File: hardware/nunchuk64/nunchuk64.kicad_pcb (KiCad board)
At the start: 2 copper layers, 50 x 41.6 mm, 40 parts, among them J1 DB9_Female, J2 DB9_Female, J3 Conn_02x03_Odd_Even, P1 CONN_WII, P2 CONN_WII, Q1 BSS138, Q2 BSS138, Q3 BSS138, Q4 BSS138, SW1 SW_Push, U1 AMS1117-3V3, U2 ATMEGA328P-AU

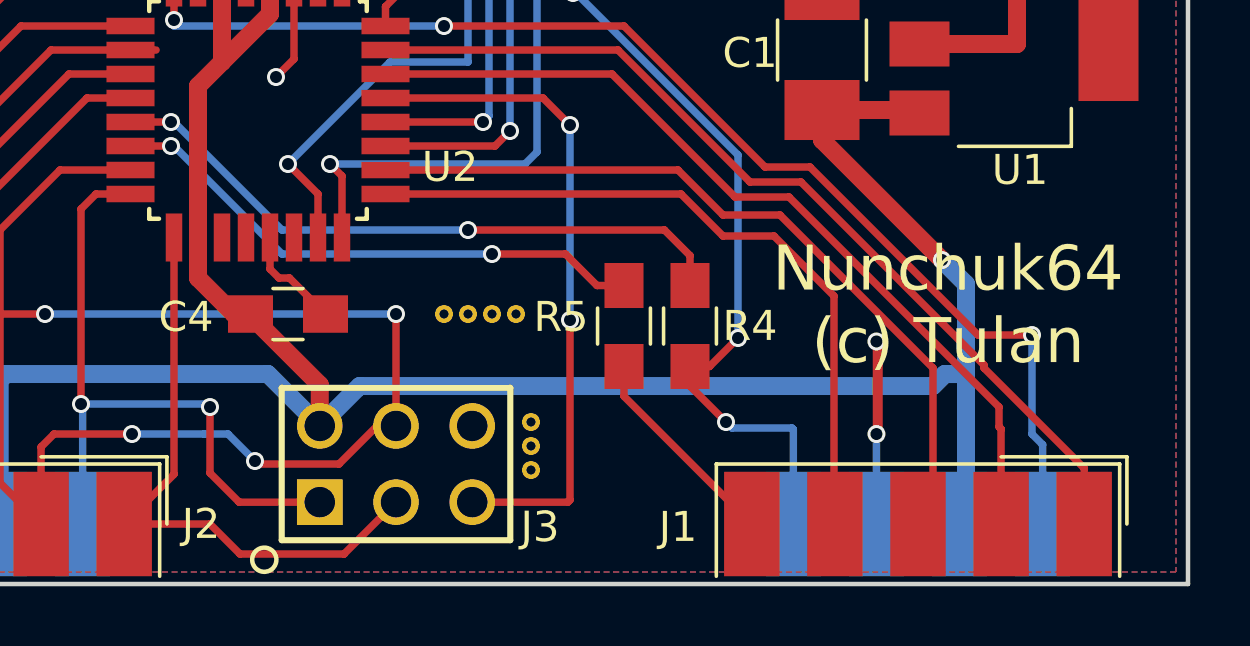
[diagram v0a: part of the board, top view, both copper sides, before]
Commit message: added cosmetic change in layout
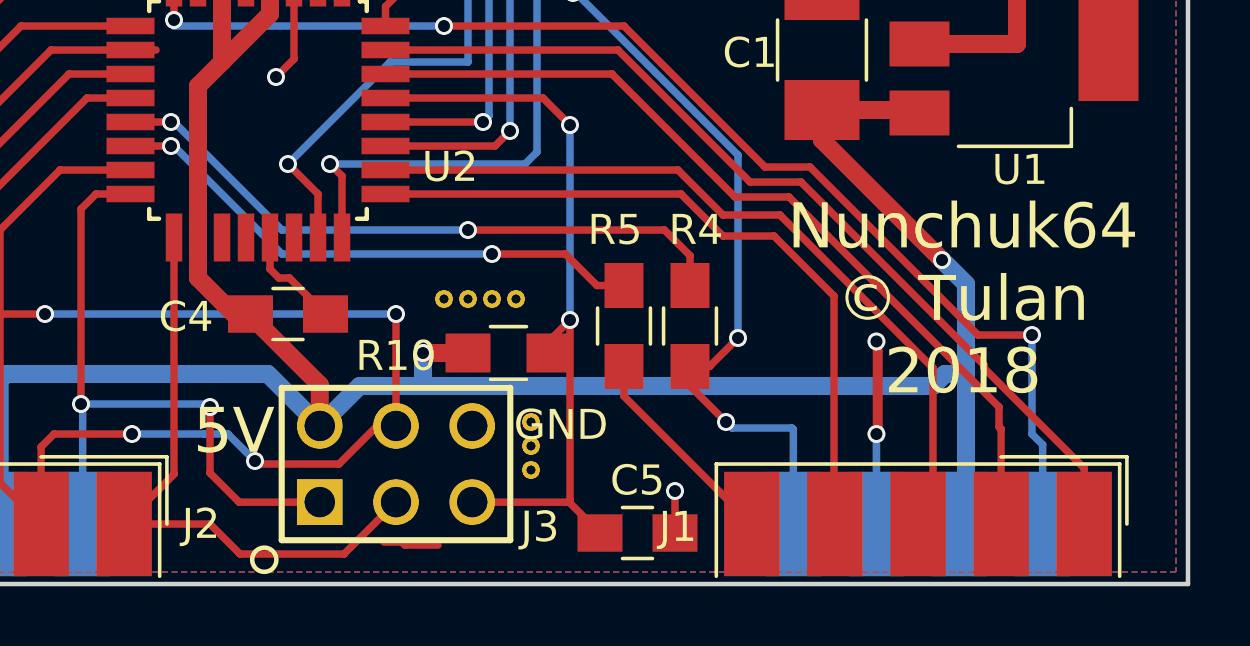
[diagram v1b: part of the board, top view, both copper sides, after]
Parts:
- added C5: 100nF, Capacitors_SMD:C_0805_HandSoldering, F.Cu at (108.0, 111.9)
- added R10: 10k, Resistors_SMD:R_0805_HandSoldering, F.Cu at (103.8, 105.9)
- moved ? 0.50 mm to (103.2, 104.1)
- moved ? 0.50 mm to (104.0, 104.1)
- moved ? 0.50 mm to (101.6, 104.1)
- moved ? 0.50 mm to (102.4, 104.1)
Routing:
- net /RESET: track 22.3 -> 25.2 mm
- net +5V: track 82.4 -> 85.0 mm, vias 1 -> 2
- net (no net): track 0.00 -> 1.84 mm
- net GND: track 23.6 -> 25.0 mm, vias 4 -> 5
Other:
- board text added: "5V"
- board text added: "GND"
- board text added: "Nunchuk64 © Tulan 2018"
- board text removed: "Nunchuk64 (c) Tulan"
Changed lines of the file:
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@@
 (kicad_pcb (version 4) (host pcbnew 4.0.7-e2-6376~58~ubuntu17.04.1)
   (general
-    (links 89)
-    (no_connects 0)
-    (area 69.224999 69.666999 133.575001 129.535)
+    (links 93)
+    (no_connects 1)
+    (area 76.324999 71.924999 126.475001 113.675001)
     (thickness 1.6)
-    (drawings 10)
-    (tracks 350)
+    (drawings 12)
+    (tracks 363)
     (zones 0)
-    (modules 40)
+    (modules 42)
     (nets 42)
   )
@@
     (tags "resistor 0805")
     (attr smd)
-    (fp_text reference R4 (at 0 -2 360) (layer F.SilkS)
+    (fp_text reference R4 (at -3.2 -0.2 360) (layer F.SilkS)
       (effects (font (size 1 1) (thickness 0.15)))
     )
@@
     (tags "resistor 0805")
     (attr smd)
-    (fp_text reference R5 (at -0.3 2.1 360) (layer F.SilkS)
+    (fp_text reference R5 (at -3.2 0.3 360) (layer F.SilkS)
       (effects (font (size 1 1) (thickness 0.15)))
     )
@@
   )
   (module nunchuk_commodore:VIA-0.6mm (layer F.Cu)
-    (at 101.6 104.6)
+    (at 101.6 104.1)
     (fp_text reference "" (at 0 1.524) (layer F.SilkS) hide
       (effects (font (size 1 1) (thickness 0.15)))
@@
   )
   (module nunchuk_commodore:VIA-0.6mm (layer F.Cu)
-    (at 102.4 104.6)
+    (at 102.4 104.1)
     (fp_text reference "" (at 0 1.524) (layer F.SilkS) hide
       (effects (font (size 1 1) (thickness 0.15)))
@@
   )
   (module nunchuk_commodore:VIA-0.6mm (layer F.Cu)
-    (at 103.2 104.6)
+    (at 103.2 104.1)
     (fp_text reference "" (at 0 1.524) (layer F.SilkS) hide
       (effects (font (size 1 1) (thickness 0.15)))
@@
   )
   (module nunchuk_commodore:VIA-0.6mm (layer F.Cu)
-    (at 104 104.6)
+    (at 104 104.1)
     (fp_text reference "" (at 0 1.524) (layer F.SilkS) hide
       (effects (font (size 1 1) (thickness 0.15)))
@@
       (net 8 GND) (zone_connect 2))
   )
-  (gr_text "Nunchuk64\n(c) Tulan" (at 118.4 104.3) (layer F.SilkS)
+  (module Capacitors_SMD:C_0805_HandSoldering (layer F.Cu)
+    (at 108.05 111.9)
+    (descr "Capacitor SMD 0805, hand soldering")
+    (tags "capacitor 0805")
+    (attr smd)
+    (fp_text reference C5 (at 0 -1.75) (layer F.SilkS)
+      (effects (font (size 1 1) (thickness 0.15)))
+    )
+    (fp_text value 100nF (at 0 1.75) (layer F.Fab)
+      (effects (font (size 1 1) (thickness 0.15)))
+    )
+    (fp_text user %R (at 0 -1.75) (layer F.Fab)
+      (effects (font (size 1 1) (thickness 0.15)))
+    )
+    (fp_line (start -1 0.62) (end -1 -0.62) (layer F.Fab) (width 0.1))
+    (fp_line (start 1 0.62) (end -1 0.62) (layer F.Fab) (width 0.1))
+    (fp_line (start 1 -0.62) (end 1 0.62) (layer F.Fab) (width 0.1))
+    (fp_line (start -1 -0.62) (end 1 -0.62) (layer F.Fab) (width 0.1))
+    (fp_line (start 0.5 -0.85) (end -0.5 -0.85) (layer F.SilkS) (width 0.12))
+    (fp_line (start -0.5 0.85) (end 0.5 0.85) (layer F.SilkS) (width 0.12))
+    (fp_line (start -2.25 -0.88) (end 2.25 -0.88) (layer F.CrtYd) (width 0.05))
+    (fp_line (start -2.25 -0.88) (end -2.25 0.87) (layer F.CrtYd) (width 0.05))
+    (fp_line (start 2.25 0.87) (end 2.25 -0.88) (layer F.CrtYd) (width 0.05))
+    (fp_line (start 2.25 0.87) (end -2.25 0.87) (layer F.CrtYd) (width 0.05))
+    (pad 1 smd rect (at -1.25 0) (size 1.5 1.25) (layers F.Cu F.Paste F.Mask)
+      (net 35 /RESET))
+    (pad 2 smd rect (at 1.25 0) (size 1.5 1.25) (layers F.Cu F.Paste F.Mask)
+      (net 8 GND))
+    (model Capacitors_SMD.3dshapes/C_0805.wrl
+      (at (xyz 0 0 0))
+      (scale (xyz 1 1 1))
+      (rotate (xyz 0 0 0))
+    )
+  )
+  (module Resistors_SMD:R_0805_HandSoldering (layer F.Cu)
+    (at 103.75 105.9)
+    (descr "Resistor SMD 0805, hand soldering")
+    (tags "resistor 0805")
+    (attr smd)
+    (fp_text reference R10 (at -3.75 0.1) (layer F.SilkS)
+      (effects (font (size 1 1) (thickness 0.15)))
+    )
+    (fp_text value 10k (at 0 1.75) (layer F.Fab)
+      (effects (font (size 1 1) (thickness 0.15)))
+    )
+    (fp_text user %R (at 0 0) (layer F.Fab)
+      (effects (font (size 0.5 0.5) (thickness 0.075)))
+    )
+    (fp_line (start -1 0.62) (end -1 -0.62) (layer F.Fab) (width 0.1))
+    (fp_line (start 1 0.62) (end -1 0.62) (layer F.Fab) (width 0.1))
+    (fp_line (start 1 -0.62) (end 1 0.62) (layer F.Fab) (width 0.1))
+    (fp_line (start -1 -0.62) (end 1 -0.62) (layer F.Fab) (width 0.1))
+    (fp_line (start 0.6 0.88) (end -0.6 0.88) (layer F.SilkS) (width 0.12))
+    (fp_line (start -0.6 -0.88) (end 0.6 -0.88) (layer F.SilkS) (width 0.12))
+    (fp_line (start -2.35 -0.9) (end 2.35 -0.9) (layer F.CrtYd) (width 0.05))
+    (fp_line (start -2.35 -0.9) (end -2.35 0.9) (layer F.CrtYd) (width 0.05))
+    (fp_line (start 2.35 0.9) (end 2.35 -0.9) (layer F.CrtYd) (width 0.05))
+    (fp_line (start 2.35 0.9) (end -2.35 0.9) (layer F.CrtYd) (width 0.05))
+    (pad 1 smd rect (at -1.35 0) (size 1.5 1.3) (layers F.Cu F.Paste F.Mask)
+      (net 7 +5V))
+    (pad 2 smd rect (at 1.35 0) (size 1.5 1.3) (layers F.Cu F.Paste F.Mask)
+      (net 35 /RESET))
+    (model ${KISYS3DMOD}/Resistors_SMD.3dshapes/R_0805.wrl
+      (at (xyz 0 0 0))
+      (scale (xyz 1 1 1))
+      (rotate (xyz 0 0 0))
+    )
+  )
+  (gr_text 5V (at 94.6 108.5) (layer F.SilkS)
+    (effects (font (size 1.5 1.5) (thickness 0.3)))
+  )
+  (gr_text GND (at 105.5 108.3) (layer F.SilkS)
+    (effects (font (size 1 1) (thickness 0.25)))
+  )
+  (gr_text "Nunchuk64\n© Tulan\n2018" (at 118.9 104.1) (layer F.SilkS)
     (effects (font (size 1.5 1.5) (thickness 0.3)))
   )
@@
   (gr_line (start 126.4 113.6) (end 126.4 72) (angle 90) (layer Eco1.User) (width 0.2))
   (gr_line (start 76.4 72) (end 76.4 113.6) (angle 90) (layer Eco1.User) (width 0.2))
+  (segment (start 100.3 112.3) (end 101.4 112.3) (width 0.25) (layer F.Cu) (net 0))
+  (segment (start 100.2 112.2) (end 100.3 112.3) (width 0.25) (layer F.Cu) (net 0))
+  (segment (start 99.6 112.2) (end 100.2 112.2) (width 0.25) (layer F.Cu) (net 0))
   (segment (start 122.94 111.6) (end 122.94 109.74) (width 0.25) (layer F.Cu) (net 1))
   (segment (start 122.94 109.74) (end 119.6 106.4) (width 0.25) (layer F.Cu) (net 1))
@@
   (segment (start 92.6 94.8) (end 92.6 93.55) (width 0.25) (layer F.Cu) (net 6))
   (via (at 92.6 94.8) (size 0.6) (drill 0.4) (layers F.Cu B.Cu) (net 6))
+  (segment (start 100.9 105.9) (end 102.4 105.9) (width 0.6) (layer F.Cu) (net 7))
+  (segment (start 100.9 107) (end 98.79 107) (width 0.6) (layer B.Cu) (net 7))
+  (segment (start 117.9 107) (end 100.9 107) (width 0.6) (layer B.Cu) (net 7))
+  (segment (start 100.9 107) (end 100.9 105.9) (width 0.6) (layer B.Cu) (net 7))
+  (via (at 100.9 105.9) (size 0.6) (drill 0.4) (layers F.Cu B.Cu) (net 7))
   (segment (start 118.3 106.6) (end 117.9 107) (width 0.6) (layer B.Cu) (net 7))
-  (segment (start 117.9 107) (end 98.79 107) (width 0.6) (layer B.Cu) (net 7))
   (segment (start 98.79 107) (end 97.46 108.33) (width 0.6) (layer B.Cu) (net 7))
   (segment (start 118.9 106.6) (end 118.3 106.6) (width 0.6) (layer B.Cu) (net 7))
@@
   (segment (start 94.2 96.2) (end 94.2 93.55) (width 0.6) (layer F.Cu) (net 7))
   (segment (start 93.4 102.05) (end 93.4 102.85) (width 0.25) (layer F.Cu) (net 7))
+  (via (at 109.3 110.5) (size 0.6) (drill 0.4) (layers F.Cu B.Cu) (net 8))
+  (segment (start 109.3 111.9) (end 109.3 110.5) (width 0.25) (layer F.Cu) (net 8))
   (via (at 116.015 105.515) (size 0.6) (drill 0.4) (layers F.Cu B.Cu) (net 8))
   (segment (start 116.015 108.6) (end 116.015 105.515) (width 0.25) (layer F.Cu) (net 8))
@@
   (segment (start 79.8 102.7) (end 87.5 95) (width 0.25) (layer F.Cu) (net 31))
   (segment (start 87.5 95) (end 91.15 95) (width 0.25) (layer F.Cu) (net 31))
+  (segment (start 105.1 105.9) (end 105.1 105.5) (width 0.25) (layer F.Cu) (net 35))
+  (segment (start 105.1 105.5) (end 105.8 104.8) (width 0.25) (layer F.Cu) (net 35))
+  (segment (start 105.73 110.87) (end 105.77 110.87) (width 0.25) (layer F.Cu) (net 35))
+  (segment (start 105.77 110.87) (end 106.8 111.9) (width 0.25) (layer F.Cu) (net 35))
   (segment (start 105.8 104.8) (end 105.8 110.8) (width 0.25) (layer F.Cu) (net 35))
   (segment (start 105.8 110.8) (end 105.73 110.87) (width 0.25) (layer F.Cu) (net 35))

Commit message: changed layout a bit
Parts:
- moved R10 0.75 mm to (104.5, 105.9)
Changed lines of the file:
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@@
   (general
     (links 93)
-    (no_connects 1)
+    (no_connects 0)
     (area 76.324999 71.924999 126.475001 113.675001)
     (thickness 1.6)
     (drawings 12)
-    (tracks 363)
+    (tracks 364)
     (zones 0)
     (modules 42)
@@
   )
   (module Resistors_SMD:R_0805_HandSoldering (layer F.Cu)
-    (at 103.75 105.9)
+    (at 104.5 105.9)
     (descr "Resistor SMD 0805, hand soldering")
     (tags "resistor 0805")
@@
   (segment (start 92.6 94.8) (end 92.6 93.55) (width 0.25) (layer F.Cu) (net 6))
   (via (at 92.6 94.8) (size 0.6) (drill 0.4) (layers F.Cu B.Cu) (net 6))
-  (segment (start 100.9 105.9) (end 102.4 105.9) (width 0.6) (layer F.Cu) (net 7))
+  (segment (start 102 105.9) (end 103.2 105.9) (width 0.6) (layer F.Cu) (net 7))
+  (segment (start 117.9 107) (end 102 107) (width 0.6) (layer B.Cu) (net 7))
+  (segment (start 102 105.9) (end 102 107) (width 0.6) (layer B.Cu) (net 7))
+  (segment (start 102 107) (end 100.9 107) (width 0.6) (layer B.Cu) (net 7))
   (segment (start 100.9 107) (end 98.79 107) (width 0.6) (layer B.Cu) (net 7))
-  (segment (start 117.9 107) (end 100.9 107) (width 0.6) (layer B.Cu) (net 7))
-  (segment (start 100.9 107) (end 100.9 105.9) (width 0.6) (layer B.Cu) (net 7))
-  (via (at 100.9 105.9) (size 0.6) (drill 0.4) (layers F.Cu B.Cu) (net 7))
+  (via (at 102 105.9) (size 0.6) (drill 0.4) (layers F.Cu B.Cu) (net 7))
   (segment (start 118.3 106.6) (end 117.9 107) (width 0.6) (layer B.Cu) (net 7))
   (segment (start 98.79 107) (end 97.46 108.33) (width 0.6) (layer B.Cu) (net 7))
@@
   (segment (start 79.8 102.7) (end 87.5 95) (width 0.25) (layer F.Cu) (net 31))
   (segment (start 87.5 95) (end 91.15 95) (width 0.25) (layer F.Cu) (net 31))
-  (segment (start 105.1 105.9) (end 105.1 105.5) (width 0.25) (layer F.Cu) (net 35))
-  (segment (start 105.1 105.5) (end 105.8 104.8) (width 0.25) (layer F.Cu) (net 35))
+  (segment (start 105.8 104.8) (end 105.8 105.85) (width 0.25) (layer F.Cu) (net 35))
+  (segment (start 105.8 105.85) (end 105.85 105.9) (width 0.25) (layer F.Cu) (net 35))
   (segment (start 105.73 110.87) (end 105.77 110.87) (width 0.25) (layer F.Cu) (net 35))
   (segment (start 105.77 110.87) (end 106.8 111.9) (width 0.25) (layer F.Cu) (net 35))

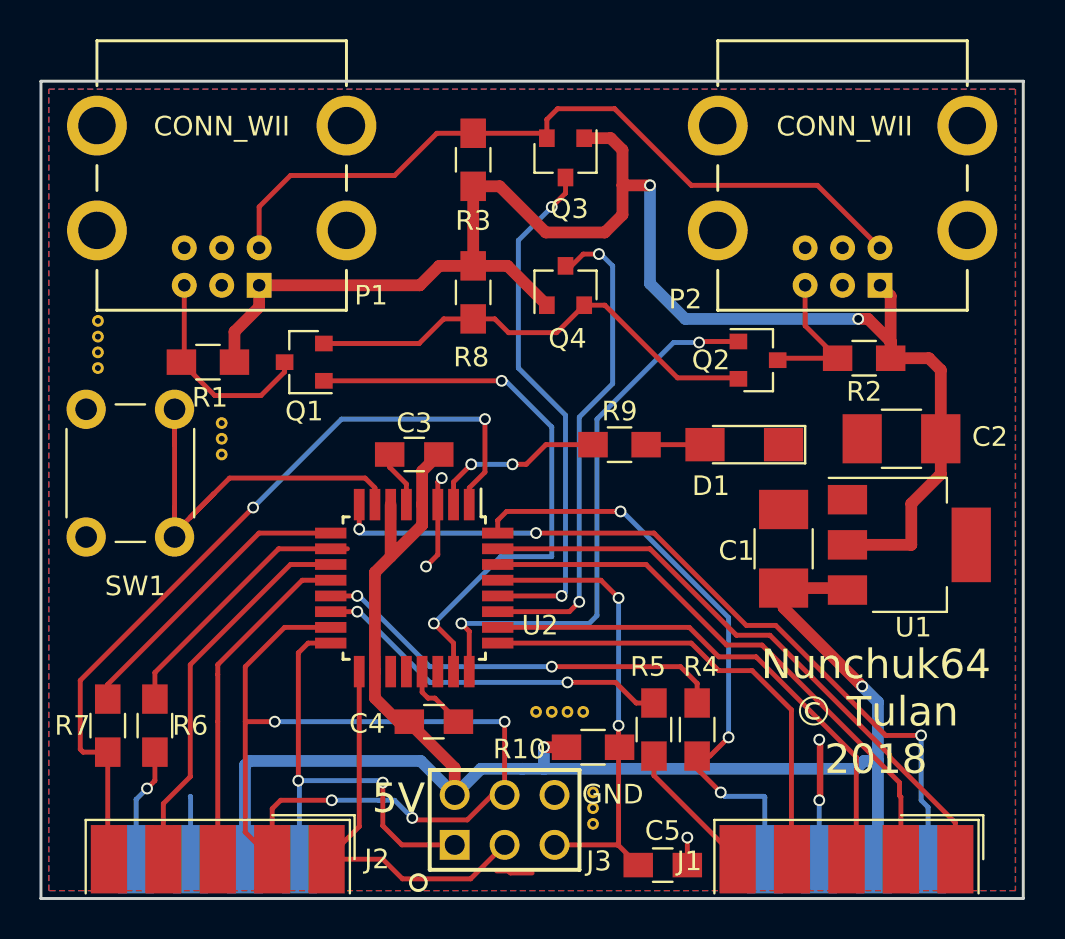
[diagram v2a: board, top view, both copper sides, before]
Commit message: Created fingers inside Connectors-Wii:CONN_WII for those hard to get connectors
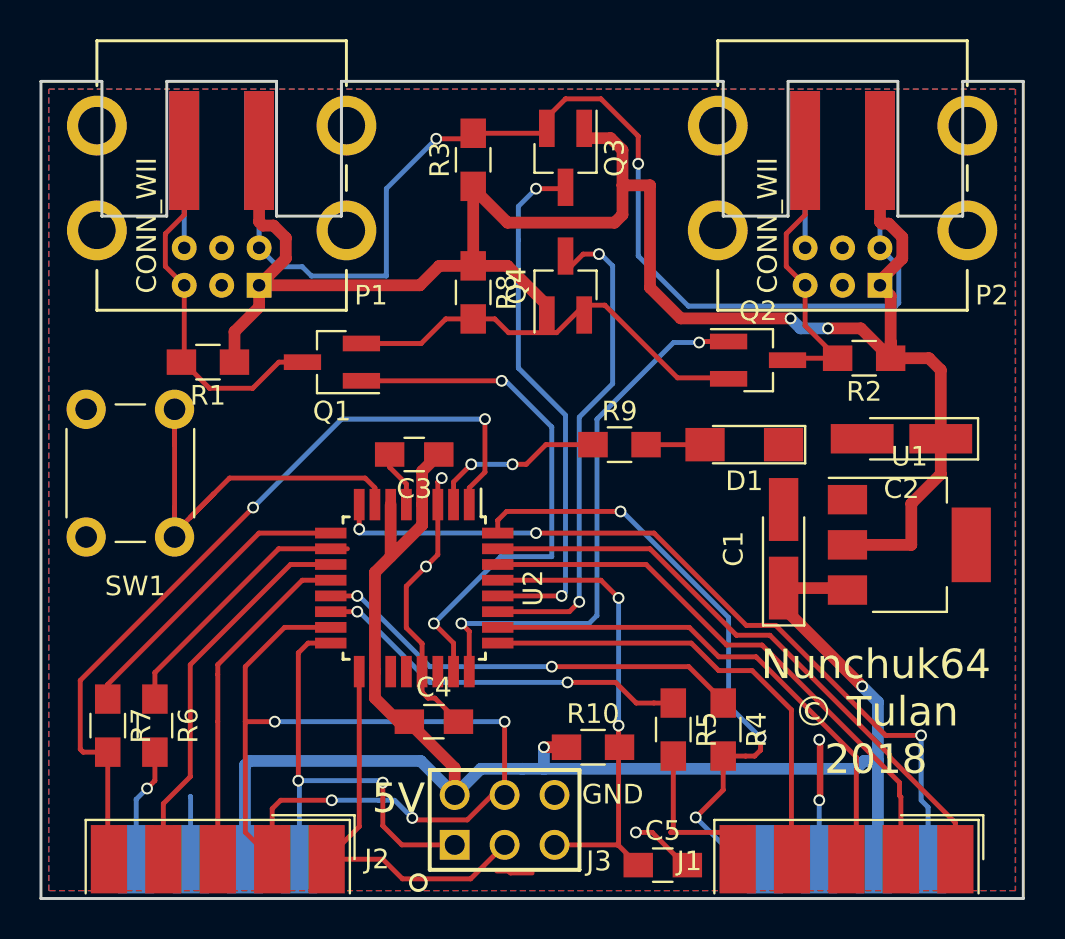
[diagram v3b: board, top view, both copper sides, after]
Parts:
- removed ? (x14): VIA-0.6mm, nunchuk_commodore:VIA-0.6mm
- C1, C2: footprint Capacitors_SMD:C_1210_HandSoldering -> Capacitors_Tantalum_SMD:CP_Tantalum_Case-A_EIA-3216-18_Hand
- P1, P2: footprint Connector_Wii:CONN_WII -> Connectors_WII:CONN_WII
- Q1, Q2, Q3, Q4: footprint TO_SOT_Packages_SMD:SOT-23 -> TO_SOT_Packages_SMD:SOT-23_Handsoldering
- moved Q1 1.41 mm to (91.2, 86.3)
- moved R4 1.33 mm to (111.1, 105.0)
- moved R5 0.98 mm to (108.6, 105.0)
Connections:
- U1 pad 4: Net-(U1-Pad4) -> (no net)
- U2 pad 19: Net-(U2-Pad19) -> (no net)
- U2 pad 20: Net-(U2-Pad20) -> (no net)
- U2 pad 22: Net-(U2-Pad22) -> (no net)
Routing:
- net /SCL: track 39.5 -> 61.9 mm, vias 0 -> 2
- net GND: track 25.0 -> 42.9 mm
- net +3V3: track 79.0 -> 95.5 mm
- net /SDA1: track 10.9 -> 19.4 mm
- net /SDA2: track 7.49 -> 15.1 mm
- net /Pot_AX: track 30.8 -> 33.6 mm
- net /SDA: track 24.0 -> 22.1 mm
- net /SEL1: track 29.4 -> 27.5 mm
- net /Pot_AY: track 7.10 -> 8.47 mm
- net /SCL_: track 26.6 -> 27.8 mm
- net /Pot_AY_: track 18.4 -> 19.4 mm
- net /Pot_AX_: track 21.5 -> 22.3 mm
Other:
- outline, holes or cut-outs redrawn

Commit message: Removed holes. Widen edge connector.
allpcb didn't approve halfplated holes at the same price.
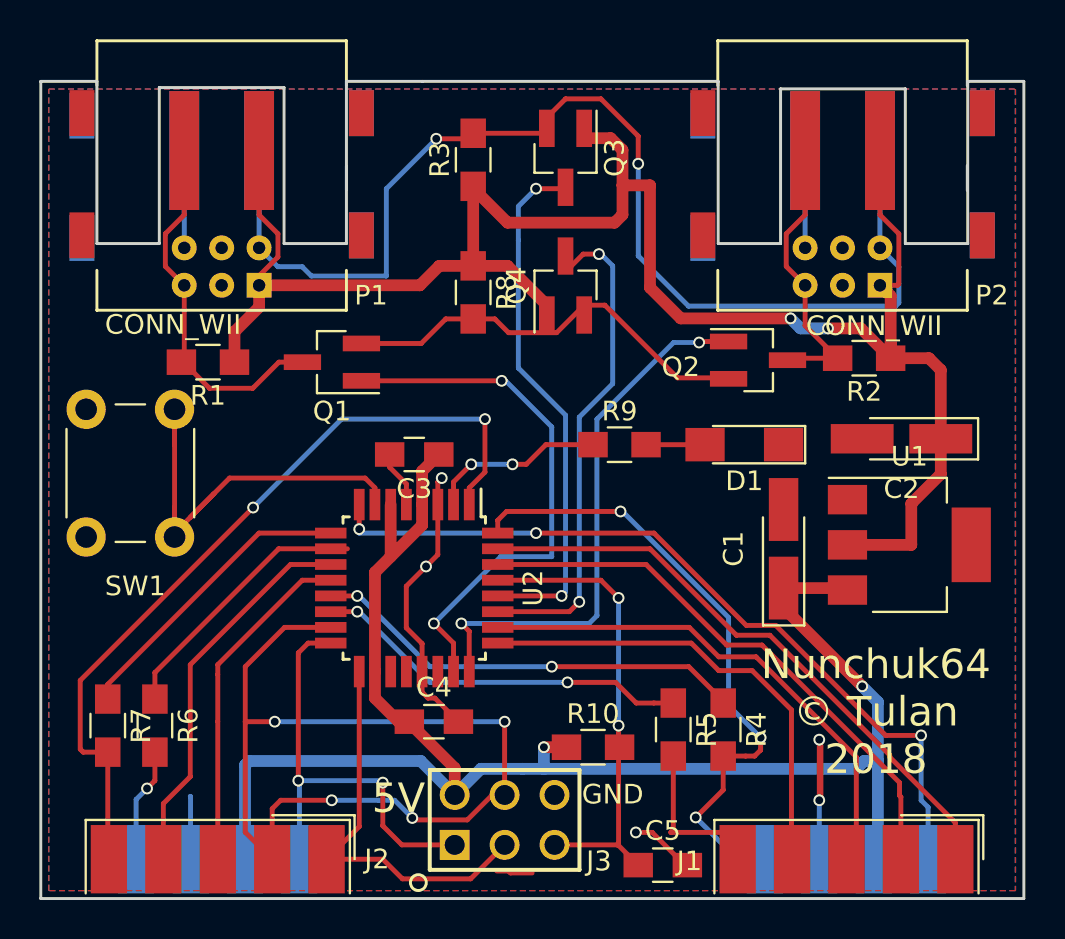
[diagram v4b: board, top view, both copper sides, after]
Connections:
- P1 pad 3: Net-(P1-Pad3) -> (no net)
- P1 pad 4: Net-(P1-Pad4) -> (no net)
- P2 pad 3: Net-(P2-Pad3) -> (no net)
- P2 pad 4: Net-(P2-Pad4) -> (no net)
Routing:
- net +3V3: track 95.5 -> 97.5 mm
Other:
- outline, holes or cut-outs redrawn
